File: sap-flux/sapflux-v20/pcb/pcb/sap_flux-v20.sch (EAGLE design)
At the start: 93 parts, among them J1 CON_01X02-0.2"_POL, J2 CON_01X02TINY, J3 CON_01X02TINY, J4 CON_01X02TINY, J5 CON_01X02TINY, Q1 Nfet, Q2 nfet, Q3 pfet, U1 ADP2503, U2 MCP73871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

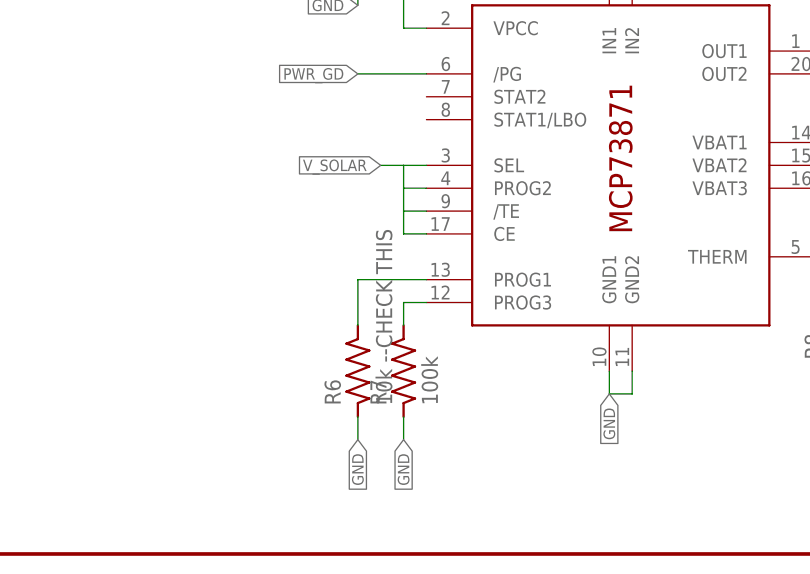
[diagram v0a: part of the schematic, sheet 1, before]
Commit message: added test data
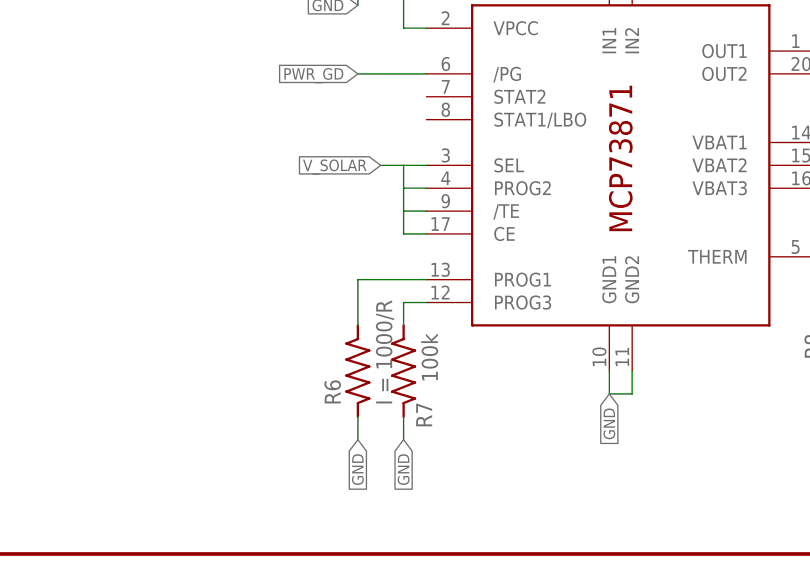
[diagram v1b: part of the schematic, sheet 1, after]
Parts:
- R6: value 10k --CHECK THIS -> I = 1000/R
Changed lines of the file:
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@@
 <attribute name="PARTNO" value="RC0603FR-07100KL"/>
 </part>
-<part name="R6" library="My_Passives" deviceset="RESISTOR" device="0603-N" value="10k --CHECK THIS">
+<part name="R6" library="My_Passives" deviceset="RESISTOR" device="0603-N" value="I = 1000/R">
 <attribute name="PARTNO" value="RC0603FR-0710KL"/>
 </part>
@@
 <instance part="C12" gate="G$1" x="205.74" y="50.8"/>
 <instance part="U2" gate="G$1" x="68.58" y="43.18"/>
-<instance part="R7" gate="G$1" x="45.72" y="20.32" rot="R90"/>
+<instance part="R7" gate="G$1" x="45.72" y="20.32" smashed="yes" rot="R90">
+<attribute name="NAME" x="48.895" y="13.97" size="1.778" layer="95" rot="R90"/>
+<attribute name="VALUE" x="49.53" y="19.05" size="1.778" layer="95" rot="R90"/>
+</instance>
 <instance part="R6" gate="G$1" x="40.64" y="20.32" rot="R90"/>
 <instance part="R8" gate="G$1" x="93.98" y="25.4" rot="R90"/>

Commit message: checked all part numbers. Minor modifications to bottom text layer
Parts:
- C32: value (none) -> 0.1uF; PARTNO (none) -> CC0603KRX7R7BB104
- Q2: PARTNO (none) -> BSS138
- Q3: PARTNO (none) -> IRLML2244TRPBF
- R22: PARTNO (none) -> RC0603FR-07100KL
- R23: PARTNO (none) -> RC0603FR-072K2L
- R25: PARTNO (none) -> RC0603FR-074K7L
- R6: value I = 1000/R -> 2k; PARTNO RC0603FR-0710KL -> RC0603FR-072KL
- R8: value 10k --CHECK THIS -> 10k
- SJ1, SJ2, SJ3, SJ4: PARTNO (none) -> NA
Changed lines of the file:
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@@
 <attribute name="PARTNO" value="RC0603FR-07100KL"/>
 </part>
-<part name="R6" library="My_Passives" deviceset="RESISTOR" device="0603-N" value="I = 1000/R">
-<attribute name="PARTNO" value="RC0603FR-0710KL"/>
-</part>
-<part name="R8" library="My_Passives" deviceset="RESISTOR" device="0603-N" value="10k --CHECK THIS">
+<part name="R6" library="My_Passives" deviceset="RESISTOR" device="0603-N" value="2k">
+<attribute name="PARTNO" value="RC0603FR-072KL"/>
+</part>
+<part name="R8" library="My_Passives" deviceset="RESISTOR" device="0603-N" value="10k">
 <attribute name="PARTNO" value="RC0603FR-0710KL"/>
 </part>
@@
 <attribute name="PARTNO" value="RC0603FR-0710KL"/>
 </part>
-<part name="Q2" library="My_Descrete_Semiconductors" deviceset="MOSFET-NCHANNEL" device="SOT23-3" value="nfet"/>
-<part name="Q3" library="My_Descrete_Semiconductors" deviceset="MOSFET-PCHANNEL" device="SOT23-3" value="pfet"/>
-<part name="R22" library="My_Passives" deviceset="RESISTOR" device="0603-N" value="100k"/>
-<part name="R23" library="My_Passives" deviceset="RESISTOR" device="0603-N" value="2.2k"/>
-<part name="R25" library="My_Passives" deviceset="RESISTOR" device="0603-N" value="4.7k"/>
-<part name="C32" library="My_Passives" deviceset="CAPACITOR_NP" device="0603-N"/>
-<part name="SJ1" library="My_Connectors" deviceset="SOLDERJUMPER" device="NC"/>
-<part name="SJ2" library="My_Connectors" deviceset="SOLDERJUMPER" device="NC"/>
-<part name="SJ3" library="My_Connectors" deviceset="SOLDERJUMPER" device="NC"/>
-<part name="SJ4" library="My_Connectors" deviceset="SOLDERJUMPER" device="NC"/>
+<part name="Q2" library="My_Descrete_Semiconductors" deviceset="MOSFET-NCHANNEL" device="SOT23-3" value="nfet">
+<attribute name="PARTNO" value="BSS138"/>
+</part>
+<part name="Q3" library="My_Descrete_Semiconductors" deviceset="MOSFET-PCHANNEL" device="SOT23-3" value="pfet">
+<attribute name="PARTNO" value="IRLML2244TRPBF"/>
+</part>
+<part name="R22" library="My_Passives" deviceset="RESISTOR" device="0603-N" value="100k">
+<attribute name="PARTNO" value="RC0603FR-07100KL"/>
+</part>
+<part name="R23" library="My_Passives" deviceset="RESISTOR" device="0603-N" value="2.2k">
+<attribute name="PARTNO" value="RC0603FR-072K2L"/>
+</part>
+<part name="R25" library="My_Passives" deviceset="RESISTOR" device="0603-N" value="4.7k">
+<attribute name="PARTNO" value="RC0603FR-074K7L"/>
+</part>
+<part name="C32" library="My_Passives" deviceset="CAPACITOR_NP" device="0603-N" value="0.1uF">
+<attribute name="PARTNO" value="CC0603KRX7R7BB104"/>
+</part>
+<part name="SJ1" library="My_Connectors" deviceset="SOLDERJUMPER" device="NC">
+<attribute name="PARTNO" value="NA"/>
+</part>
+<part name="SJ2" library="My_Connectors" deviceset="SOLDERJUMPER" device="NC">
+<attribute name="PARTNO" value="NA"/>
+</part>
+<part name="SJ3" library="My_Connectors" deviceset="SOLDERJUMPER" device="NC">
+<attribute name="PARTNO" value="NA"/>
+</part>
+<part name="SJ4" library="My_Connectors" deviceset="SOLDERJUMPER" device="NC">
+<attribute name="PARTNO" value="NA"/>
+</part>
 </parts>
 <sheets>
@@
 </nets>
 </sheet>
-<sheet>
-<plain>
-</plain>
-<instances>
-</instances>
-<busses>
-</busses>
-<nets>
-</nets>
-</sheet>

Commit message: updated bottom Silk Screen
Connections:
- net GND: now also C11.NEG; no longer C11.NET
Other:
- moved on the sheet: C11
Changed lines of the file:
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@@
 <pinref part="D4" gate="G$1" pin="C"/>
 <wire x1="185.42" y1="58.42" x2="195.58" y2="58.42" width="0.1524" layer="91"/>
-<pinref part="C11" gate="G$1" pin="POS"/>
-<wire x1="195.58" y1="58.42" x2="195.58" y2="55.88" width="0.1524" layer="91"/>
+<pinref part="C12" gate="G$1" pin="1"/>
 <wire x1="195.58" y1="58.42" x2="205.74" y2="58.42" width="0.1524" layer="91"/>
-<pinref part="C12" gate="G$1" pin="1"/>
 <wire x1="205.74" y1="58.42" x2="205.74" y2="53.34" width="0.1524" layer="91"/>
 <wire x1="205.74" y1="58.42" x2="210.82" y2="58.42" width="0.1524" layer="91"/>
 <label x="210.82" y="58.42" size="1.27" layer="95" xref="yes"/>
+<pinref part="C11" gate="G$1" pin="POS"/>
+<wire x1="195.58" y1="55.88" x2="195.58" y2="58.42" width="0.1524" layer="91"/>
 </segment>
 <segment>
@@
 <segment>
 <pinref part="C12" gate="G$1" pin="2"/>
-<pinref part="C11" gate="G$1" pin="NET"/>
-<wire x1="195.58" y1="50.8" x2="195.58" y2="45.72" width="0.1524" layer="91"/>
 <wire x1="205.74" y1="45.72" x2="195.58" y2="45.72" width="0.1524" layer="91"/>
 <wire x1="195.58" y1="45.72" x2="175.26" y2="45.72" width="0.1524" layer="91"/>
@@
 <label x="175.26" y="45.72" size="1.27" layer="95" rot="R270" xref="yes"/>
 <pinref part="J1" gate="G$1" pin="PIN1"/>
+<pinref part="C11" gate="G$1" pin="NEG"/>
+<wire x1="195.58" y1="48.26" x2="195.58" y2="45.72" width="0.1524" layer="91"/>
 </segment>
 <segment>

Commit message: labeled the thermocouple connections
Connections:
- net N$1 renamed TC2_POS
- net N$2 renamed TC2_NEG
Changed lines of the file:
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@@
 <?xml version="1.0" encoding="utf-8"?>
 <!DOCTYPE eagle SYSTEM "eagle.dtd">
-<eagle version="8.0.0">
+<eagle version="8.0.1">
 <drawing>
 <settings>
@@
 </segment>
 </net>
-<net name="N$1" class="0">
+<net name="TC2_POS" class="0">
 <segment>
 <wire x1="160.02" y1="132.08" x2="160.02" y2="134.62" width="0.1524" layer="91"/>
@@
 </segment>
 </net>
-<net name="N$2" class="0">
+<net name="TC2_NEG" class="0">
 <segment>
 <wire x1="157.48" y1="132.08" x2="157.48" y2="139.7" width="0.1524" layer="91"/>
